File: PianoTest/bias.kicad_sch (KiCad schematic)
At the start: 18 parts, among them U501 DAC61402RHBR, U502 INA239AIDGSR

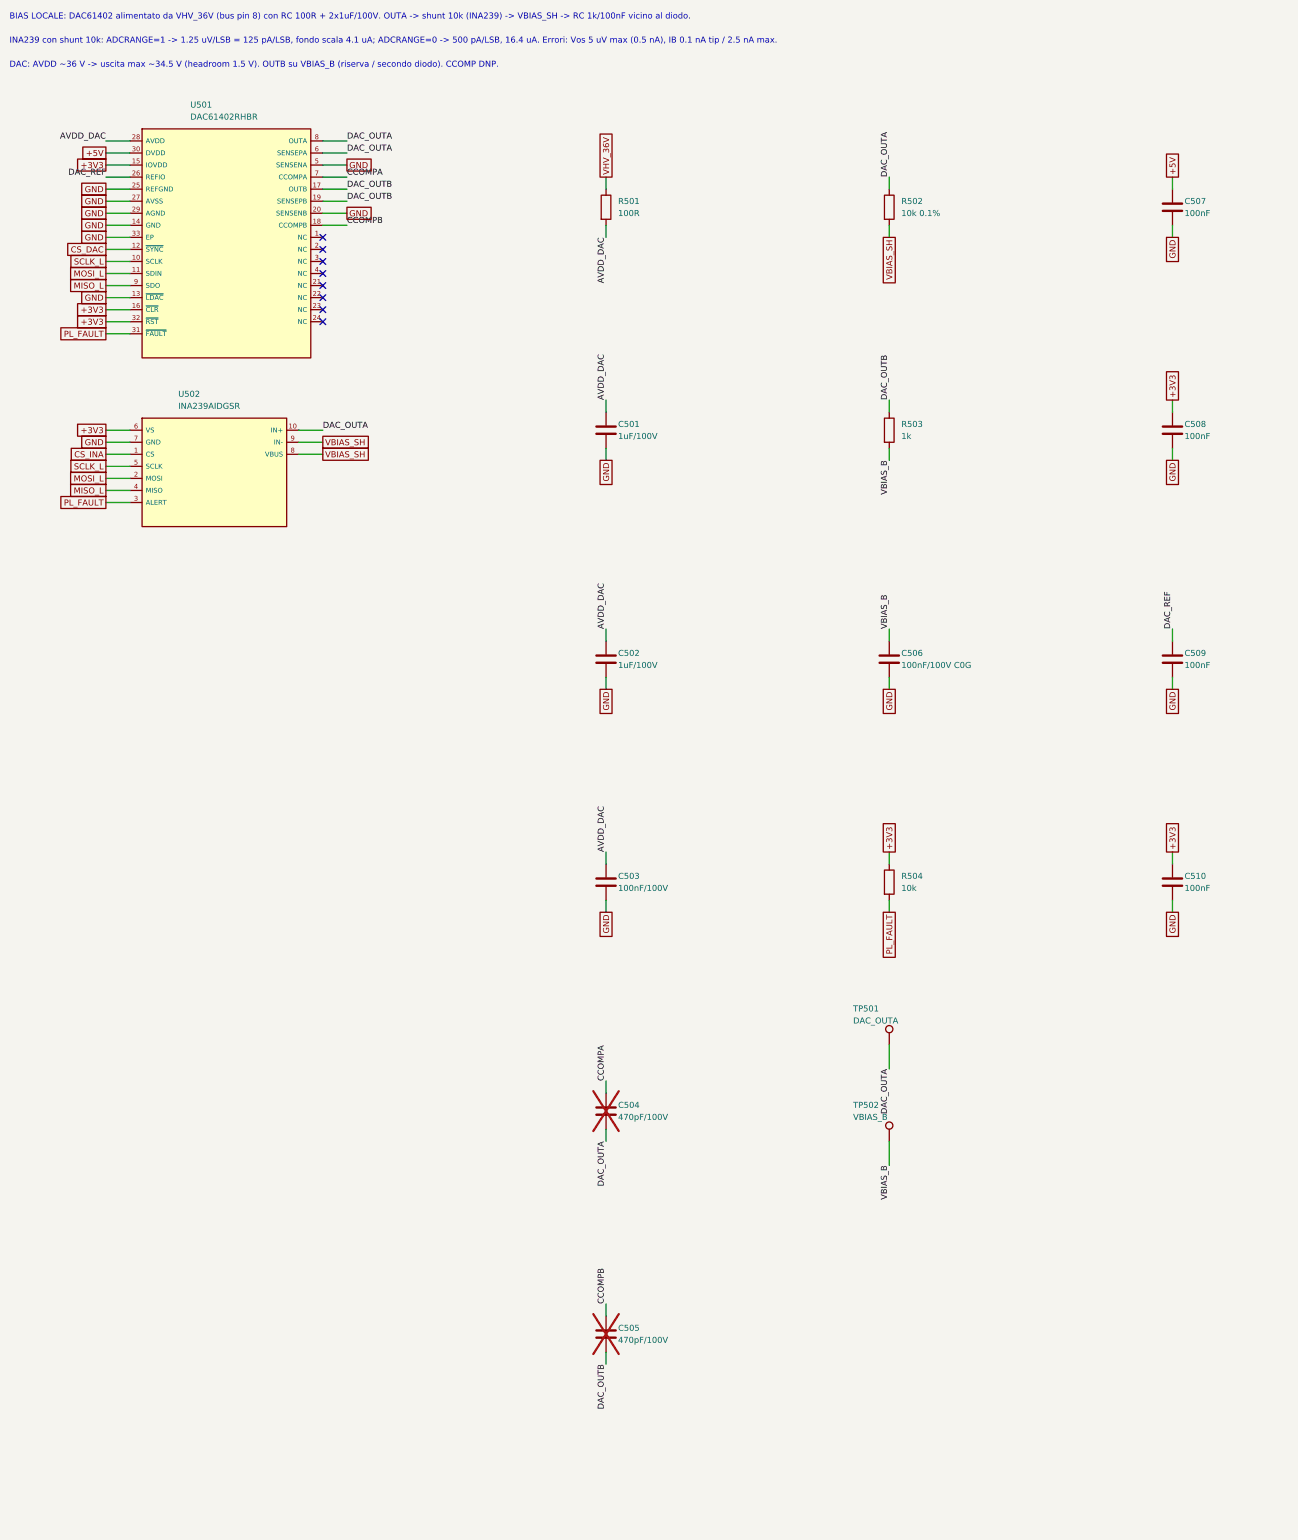
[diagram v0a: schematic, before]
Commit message: PianoTest: discriminatore, latch e rilevatore di picco
Comparatore TLV3501 su SHAPER_OUT con soglia dal canale B del DAC61402
(partitore 22k/10k, BAT54S), latch 74LVC1G74 su GPA7 dell'MCP (ALERT#),
uscita HIT su TP e SMA. Rilevatore di picco OPA2365 + BAS416 + hold 1 nF
C0G prima dell'ADS8326, con reset da accesso SPI all'indirizzo 3 e
ponticello 0R per scavalcarlo. Trigger del LED dallo strobe dell'indirizzo 4.
Articolo: sezione 3.1 (formatore e acquisizione) aggiornata e ricompilata.
ERC 0.

Co-Authored-By: Claude Opus 5.5 (1M context) <noreply@anthropic.com>
Claude-Session: https://claude.ai/code/session_01J3krgWFTUEjwvCnwUp9cQn
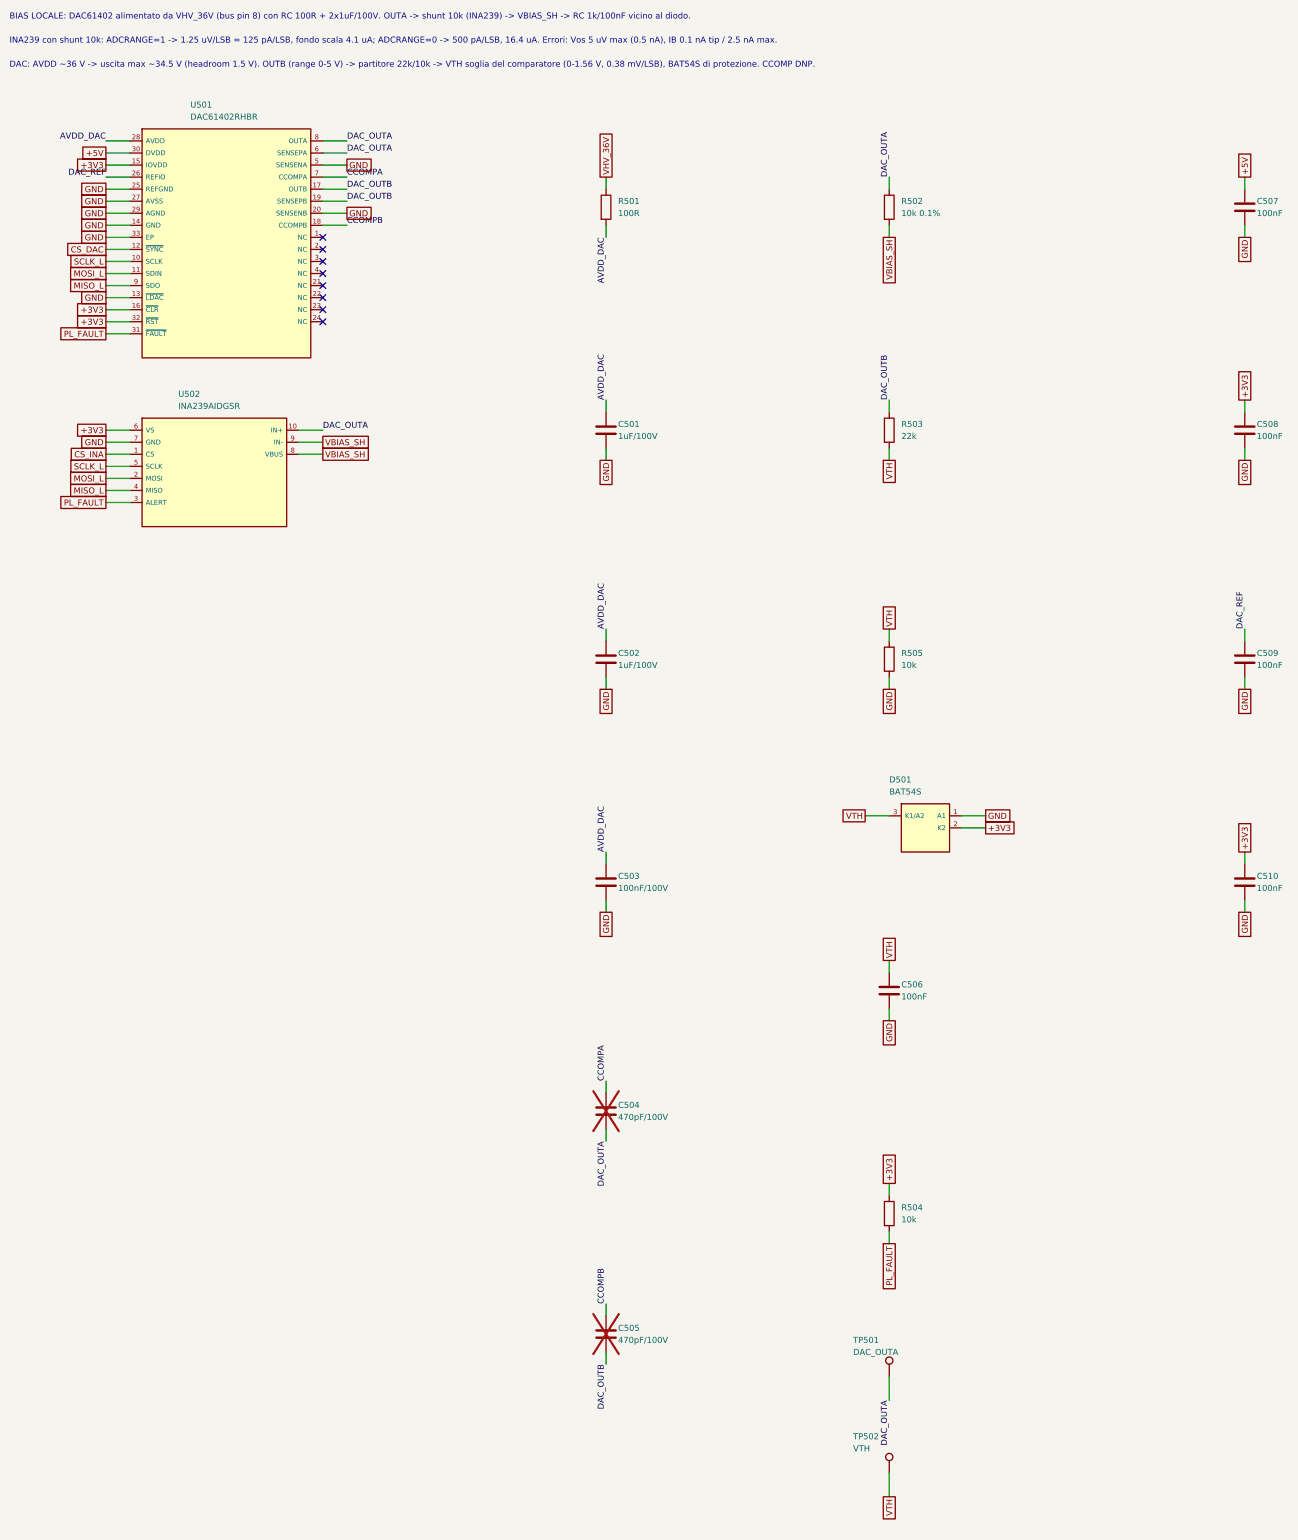
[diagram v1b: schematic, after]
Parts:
- added D501: BAT54S, Package_TO_SOT_SMD:SOT-23, symbol PianoTest:BAT54S
- added R505: 10k, Resistor_SMD:R_0603_1608Metric, symbol Device:R
- C506: value 100nF/100V C0G -> 100nF; footprint Capacitor_SMD:C_1206_3216Metric -> Capacitor_SMD:C_0603_1608Metric; MPN C3216C0G2A104J160AE -> (none)
- R503: value 1k -> 22k
- TP502: value VBIAS_B -> VTH
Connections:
- net +3V3: now also D501.2 (K2)
- net GND: now also D501.1 (A1), R505.2
- net VBIAS_B renamed VTH
- net VTH: now also D501.3 (K1/A2), R505.1
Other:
- note added: "DAC: AVDD ~36 V -> uscita max ~34.5 V (headroom 1.5 V). OUTB (range 0-5 V) -> partitore 22k/10k -> VTH soglia del comparatore (0-1.56 V, 0.38 mV/LSB), BAT54S di protezione. CCOMP DNP."
- note removed: "DAC: AVDD ~36 V -> uscita max ~34.5 V (headroom 1.5 V). OUTB su VBIAS_B (riserva / secondo diodo). CCOMP DNP."
